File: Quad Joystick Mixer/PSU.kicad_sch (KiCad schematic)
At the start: 67 parts, among them J1 Barrel_Jack_Switch, SW1 SW_DPDT_x2, U1 LM338-TO-220, U2 LM2990T-12/NOPB, U3 AP63200WU, U4 TL072, U8 MCP1755T-5002E/OT

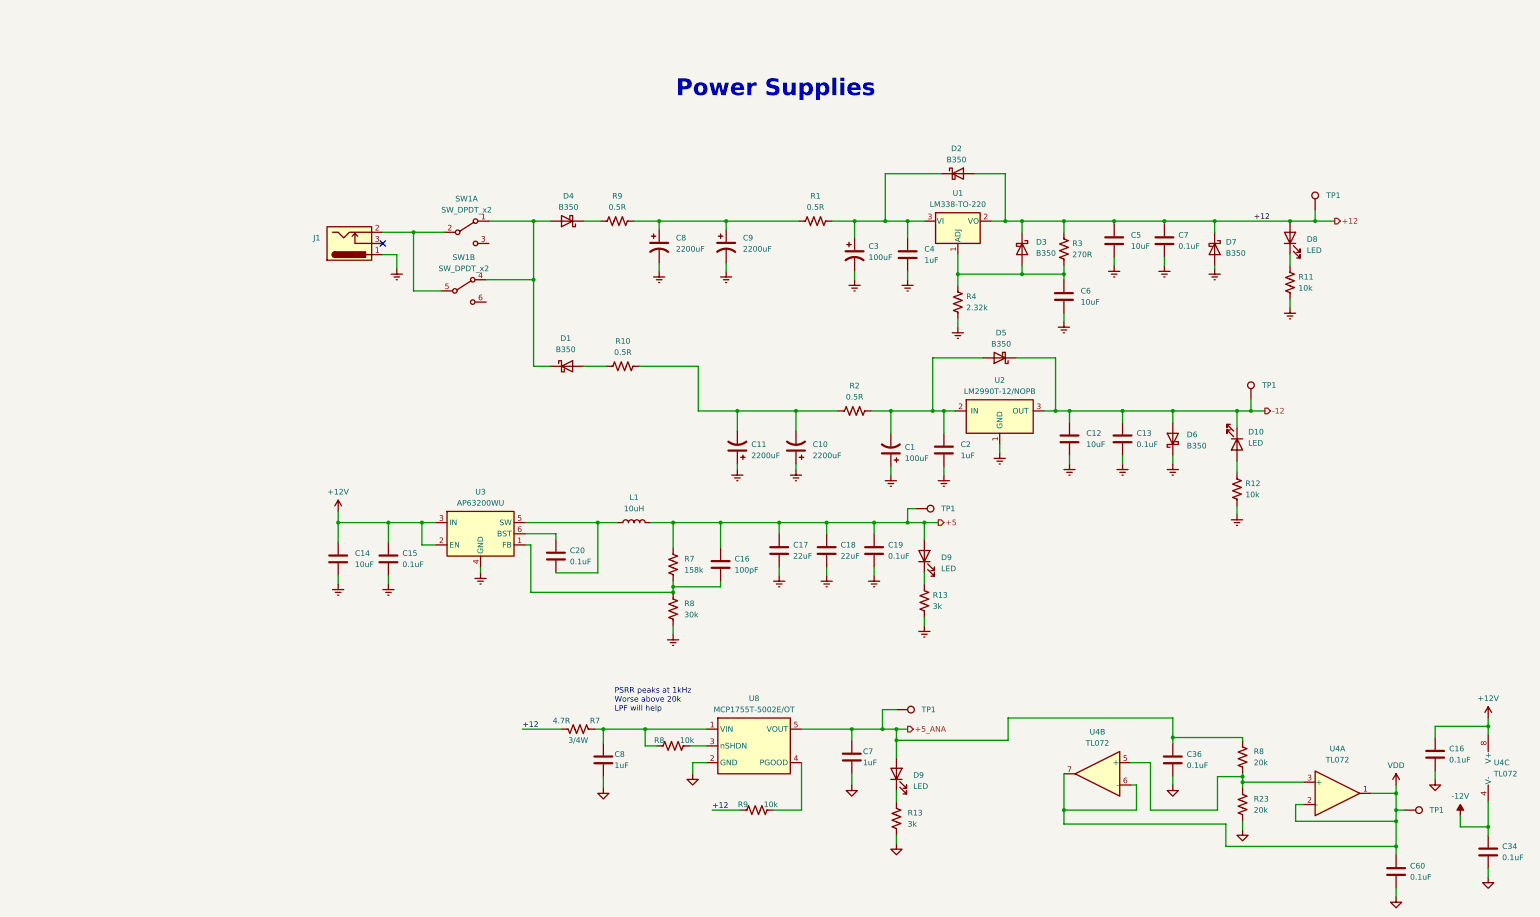
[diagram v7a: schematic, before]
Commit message: changed power supply design and everything re routed
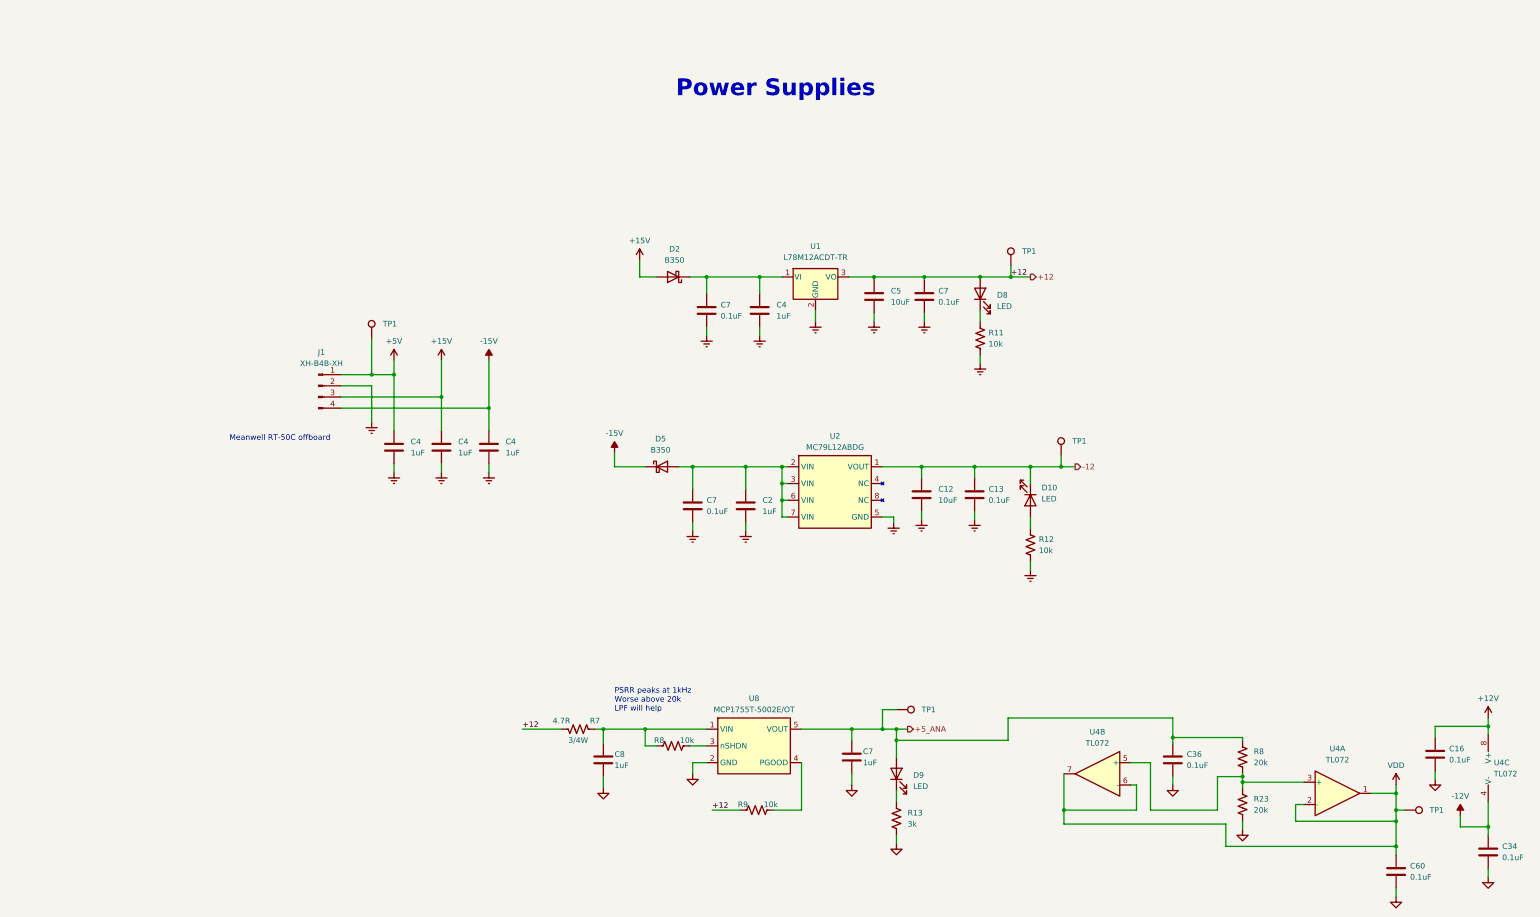
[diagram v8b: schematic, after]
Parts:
- removed C1, C3: 100uF, Capacitor_THT:CP_Radial_D8.0mm_P3.50mm, symbol Device:C_Polarized_US
- removed C10, C11, C8, C9: 2200uF, Capacitor_THT:C_Radial_D16.0mm_H25.0mm_P7.50mm, symbol Device:C_Polarized_US
- removed C14, C6: 10uF, Capacitor_SMD:C_0805_2012Metric_Pad1.18x1.45mm_HandSolder, symbol Device:C
- removed C15, C19, C20: 0.1uF, Capacitor_SMD:C_0805_2012Metric_Pad1.18x1.45mm_HandSolder, symbol Device:C
- removed C16: 100pF, Capacitor_SMD:C_0805_2012Metric_Pad1.18x1.45mm_HandSolder, symbol Device:C
- removed C17, C18: 22uF, Capacitor_SMD:C_1206_3216Metric_Pad1.33x1.80mm_HandSolder, symbol Device:C
- removed D1, D3, D4, D6, D7: B350, Diode_SMD:D_SMA_Handsoldering, symbol Diode:B350
- removed D9: LED, LED_THT:LED_D3.0mm_FlatTop, symbol Device:LED
- removed J1: Barrel_Jack_Switch, Eyewool Connectors:Love My Switches 2.1MM PCB Mount DC Jack, symbol Connector:Barrel_Jack_Switch
- removed L1: 10uH, Inductor_SMD:L_Abracon_ASPI-0630LR, symbol Device:L
- removed R1, R10, R2, R9: 0.5R, Resistor_SMD:R_2512_6332Metric_Pad1.40x3.35mm_HandSolder, symbol Device:R_US
- removed R13: 3k, Resistor_SMD:R_0805_2012Metric_Pad1.20x1.40mm_HandSolder, symbol Device:R_US
- removed R3: 270R, Resistor_SMD:R_0805_2012Metric_Pad1.20x1.40mm_HandSolder, symbol Device:R_US
- removed R4: 2.32k, Resistor_SMD:R_0805_2012Metric_Pad1.20x1.40mm_HandSolder, symbol Device:R_US
- removed R7: 158k, Resistor_SMD:R_0805_2012Metric_Pad1.20x1.40mm_HandSolder, symbol Device:R_US
- removed R8: 30k, Resistor_SMD:R_0805_2012Metric_Pad1.20x1.40mm_HandSolder, symbol Device:R_US
- removed SW1: SW_DPDT_x2, Eyewool Switches:Taiway DPDT, symbol Switch:SW_DPDT_x2
- removed U1: LM338-TO-220, Package_TO_SOT_THT:TO-220-3_Vertical, symbol Eyewool ICs:LM338-TO-220
- removed U2: LM2990T-12/NOPB, Package_TO_SOT_THT:TO-220-3_Vertical, symbol Regulator_Linear:LM2990SX-12
- removed U3: AP63200WU, Package_TO_SOT_SMD:TSOT-23-6, symbol Regulator_Switching:AP63200WU
- added C4 (x3): 1uF, Capacitor_SMD:C_0805_2012Metric_Pad1.18x1.45mm_HandSolder, symbol Device:C
- added C7 (x2): 0.1uF, Capacitor_SMD:C_0805_2012Metric_Pad1.18x1.45mm_HandSolder, symbol Device:C
- added J1: XH-B4B-XH, Connector_JST:JST_XH_B4B-XH-AM_1x04_P2.50mm_Vertical, symbol Connector:Conn_01x04_Pin
- added U1: L78M12ACDT-TR, Package_TO_SOT_SMD:TO-252-2, symbol Eyewool ICs:L78M12ACDT-TR
- added U2: MC79L12ABDG, Package_SO:SOIC-8_3.9x4.9mm_P1.27mm, symbol Eyewool ICs:MC79L12ABDG
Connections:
- net +12: now also U1.3 (VO); no longer D2.2 (A)
- net -12: now also U2.1 (VOUT); no longer D5.1 (K)
- net Earth: now also C4.2, C4.2, C4.2, C7.2, C7.2, J1.2 (Pin_2), U1.2 (GND), U2.5 (GND)
- net at C4.1, D2.1 (K): now also C7.1, U1.1 (VI)
- net at C2.1, D5.2 (A): now also C7.1, U2.2 (VIN), U2.3 (VIN), U2.6 (VIN), U2.7 (VIN)
- net +5 renamed +5V
- net +5V: now also C4.1, J1.1 (Pin_1)
- new net +15V: C4.1, D2.2 (A), J1.3 (Pin_3)
- new net -15V: C4.1, D5.1 (K), J1.4 (Pin_4)
- no-connect marks 1 -> 0
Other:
- note added: "Meanwell RT-50C offboard"
- moved on the sheet: C12, C13, C2, C4, C5, C7, D10, D2, D5, D8, R11, R12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
